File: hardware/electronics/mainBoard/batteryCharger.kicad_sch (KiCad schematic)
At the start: 63 parts, among them J23 M8AS-02PFFR-SF8001, J24 MUSBRM1C1M0, J25 S2B-PH-SM4-TB, Q1 CSD17581Q3A, Q2 CSD17581Q3A, Q3 CSD17581Q3A, Q4 CSD17581Q3A, Q5 CSD17581Q3A, U21 BQ25798

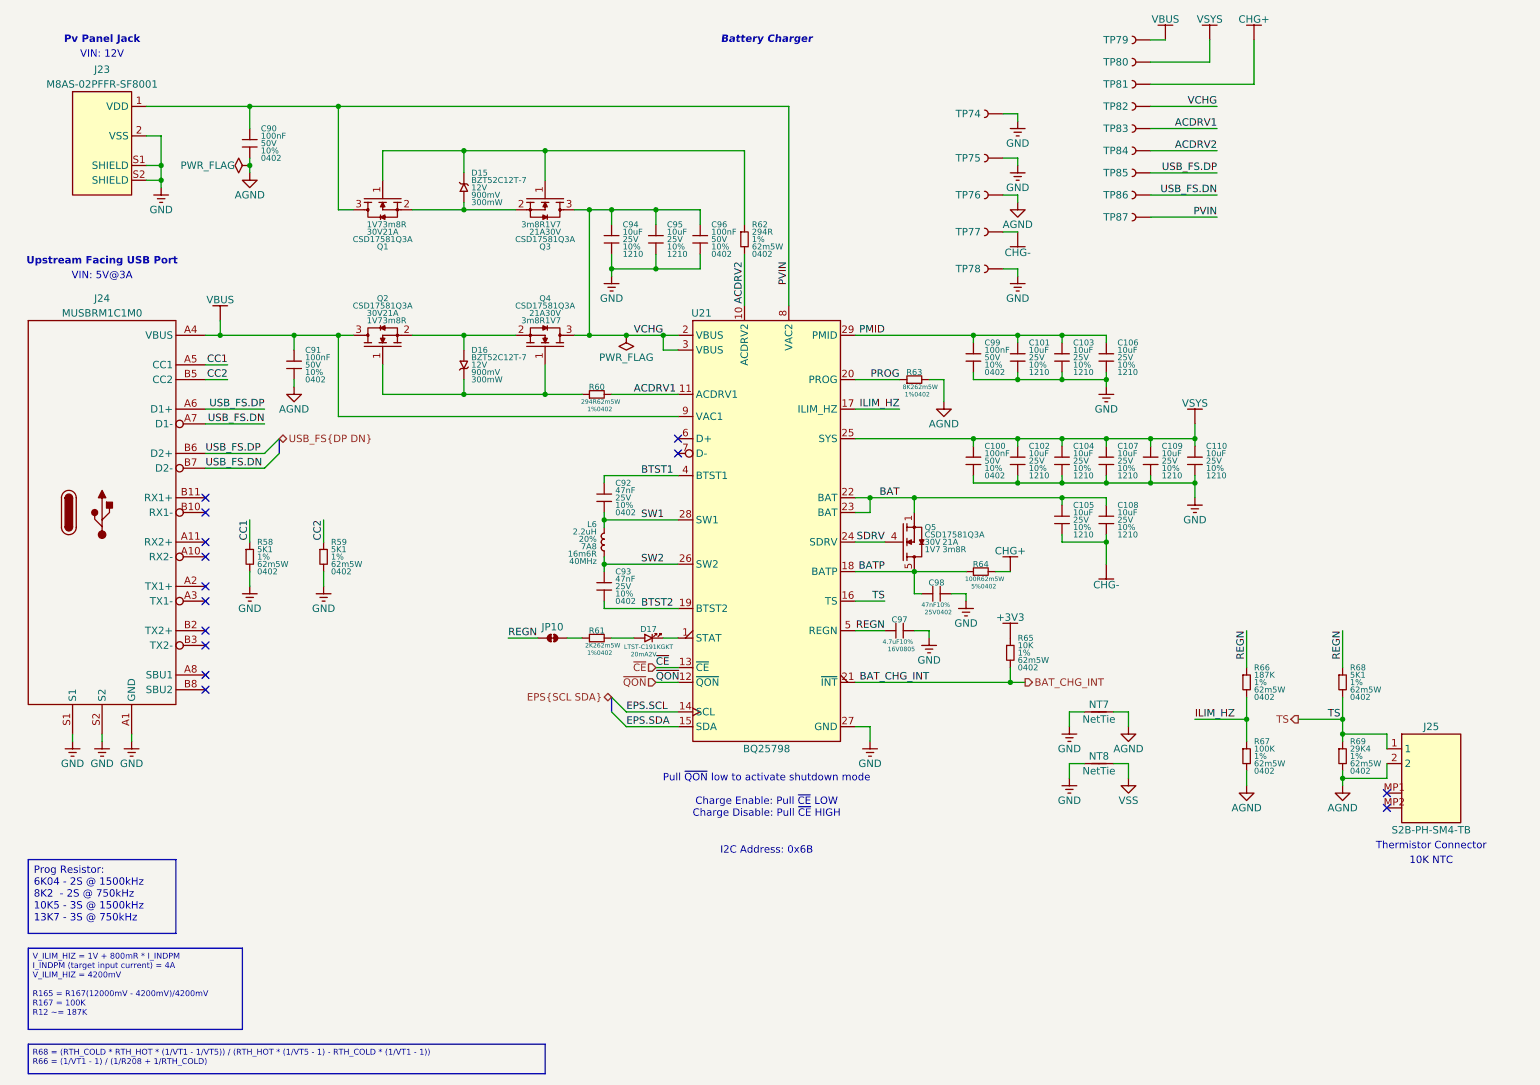
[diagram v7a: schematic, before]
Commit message: updated symbol refs
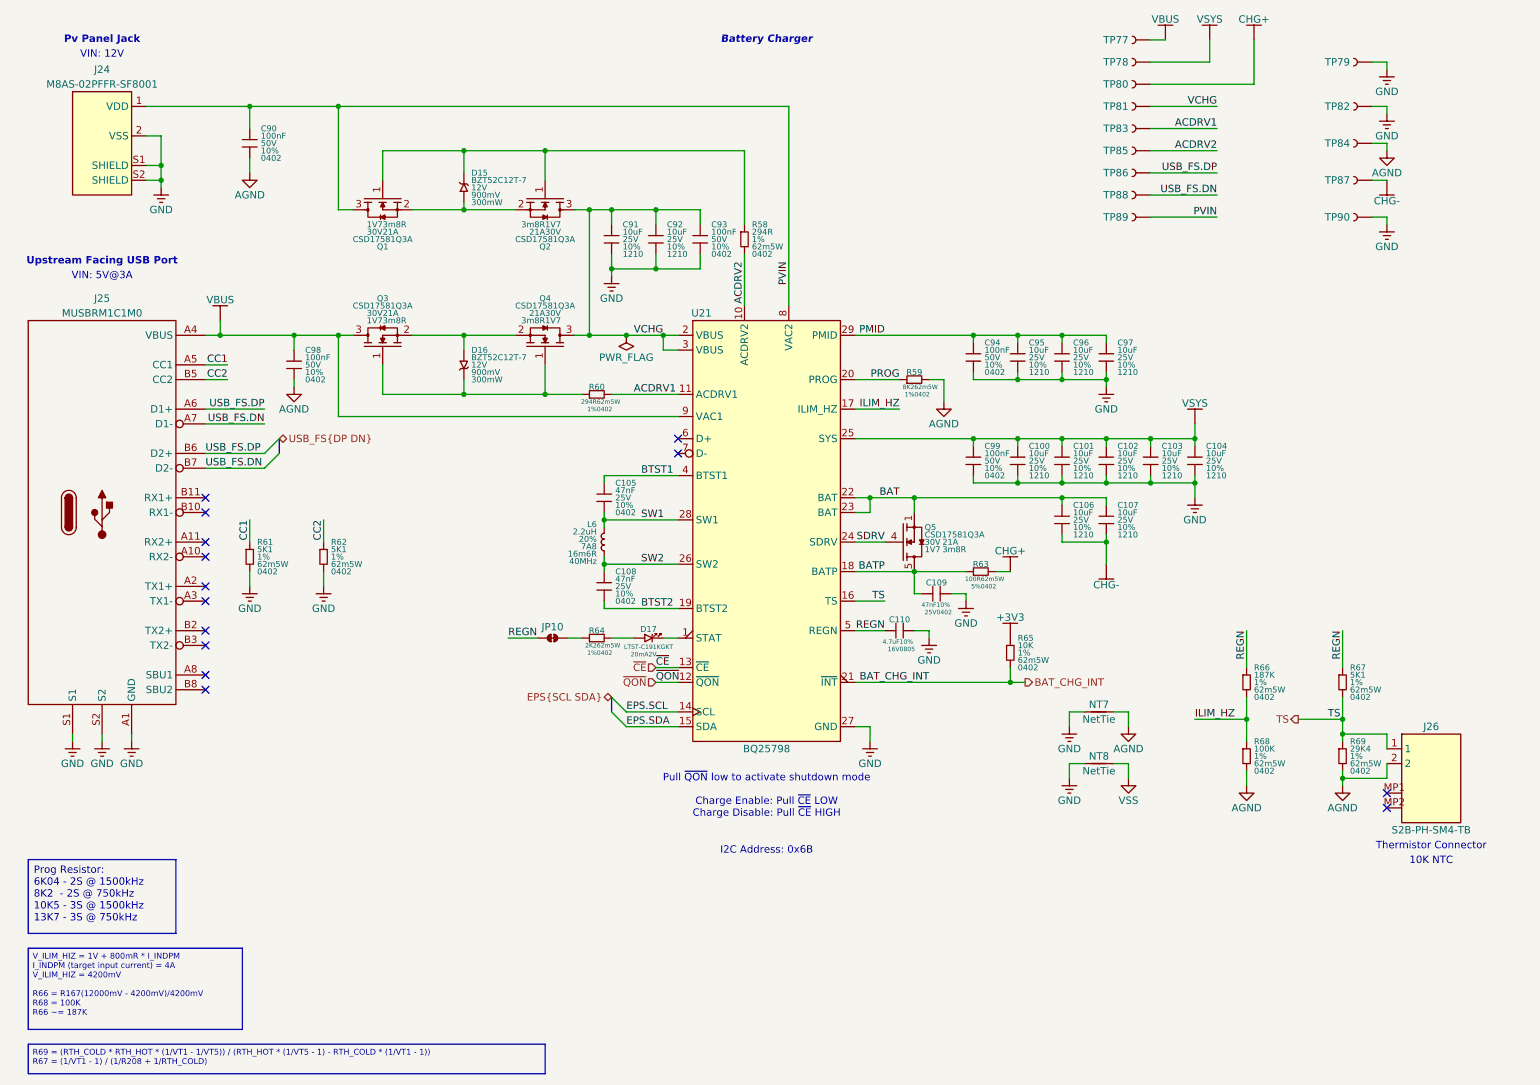
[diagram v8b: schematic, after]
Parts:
- renumbered C102 to C100, C104 to C101, C107 to C102, C109 to C103, C110 to C104, C92 to C105, C105 to C106, C108 to C107, C93 to C108, C98 to C109, C97 to C110, C94 to C91, C95 to C92, C96 to C93, C99 to C94, C101 to C95, C103 to C96, C106 to C97, C91 to C98, C100 to C99, J23 to J24, J24 to J25, J25 to J26, Q3 to Q2, Q2 to Q3, R62 to R58, R63 to R59, R58 to R61, R59 to R62, R64 to R63, R61 to R64, R68 to R67, R67 to R68, TP79 to TP77, TP80 to TP78, TP74 to TP79, TP81 to TP80, TP82 to TP81, TP75 to TP82, TP76 to TP84, TP84 to TP85, TP85 to TP86, TP77 to TP87, TP86 to TP88, TP87 to TP89, TP78 to TP90
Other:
- moved on the sheet: TP79, TP82, TP84, TP87, TP90
